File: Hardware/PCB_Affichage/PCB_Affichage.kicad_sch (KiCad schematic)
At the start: 0 parts

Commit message: finalisation PCB Rack
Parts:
- added C1, C5: 100n, Capacitor_SMD:C_0603_1608Metric_Pad1.08x0.95mm_HandSolder, symbol Device:C
- added C2: 1u, Capacitor_SMD:C_0201_0603Metric_Pad0.64x0.40mm_HandSolder, symbol Device:C
- added C3: 100u, Capacitor:Wurth-100u, symbol Device:C_Polarized
- added D1: TVS, Diode_SMD:Nexperia_DSN1608-2_1.6x0.8mm, symbol Diode:PTVS7V5Z1USK
- added D2: LED, LED_SMD:LED_0603_1608Metric_Pad1.05x0.95mm_HandSolder, symbol Device:LED
- added J1: Conn_01x03, Conn_Alim:Conn_Secteur, symbol Connector_Generic:Conn_01x03
- added R3: 2k5, Resistor_SMD:R_0603_1608Metric_Pad0.98x0.95mm_HandSolder, symbol Device:R
- added R5, R6: 2k2, Resistor_SMD:R_0603_1608Metric_Pad0.98x0.95mm_HandSolder, symbol Device:R
- added SW1: SW_SPST, Switch:Wurth_2pin_P5.0mm, symbol Switch:SW_SPST
- added U1: ~, ESP32_C3_SuperMini:C3_SuperMini, symbol ESP32_C3_SuperMini:SuperMini_1
- added U2: ~, AC_DC_module:MP-LDE06-20B05, symbol AC-DC-5V:U_1
- added U3: PCF8575DBR, Package_SO:SSOP-24_5.3x8.2mm_P0.65mm, symbol Interface_Expansion:PCF8575DBR
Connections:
- new net: D2.2 (A), R3.2
- new net +5V: C1.1, C2.1, C3.1, C5.2, D1.1 (K), R3.1, R5.1, R6.1, U1.8 (5V), U2.4 (DC+), U3.24 (VCC)
- new net Earth: J1.3 (Pin_3)
- new net GND: C1.2, C2.2, C3.2, C5.1, D1.2 (A), D2.1 (K), U1.7 (GND), U2.3 (DC-), U3.12 (GND), U3.2 (A1), U3.21 (A0), U3.3 (A2)
- new net INA1_1: U3.4 (P0)
- new net INA1_2: U3.5 (P1)
- new net INA2_1: U3.6 (P2)
- new net INA2_2: U3.7 (P3)
- new net INA3_1: U3.8 (P4)
- new net INA3_2: U3.9 (P5)
- new net INA4_1: U3.10 (P6)
- new net INA4_2: U3.11 (P7)
- new net INA5_1: U3.13 (P10)
- new net INA5_2: U3.14 (P11)
- new net INA6_1: U3.15 (P12)
- new net INA6_2: U3.16 (P13)
- new net LINE: SW1.1 (A), U2.2 (L)
- new net NEUT: J1.2 (Pin_2), U2.1 (N)
- new net On/Off: U1.14 (GPIO10)
- new net Phase: J1.1 (Pin_1), SW1.2 (B)
- new net Px: U1.9 (GPIO5)
- new net SCL: R5.2, U1.13 (GPIO9), U3.22 (SCL)
- new net SDA: R6.2, U1.12 (GPIO8), U3.23 (SDA)
- no-connect marks 0 -> 15
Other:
- note added: "Alimentation (230VAC)"
- note added: "Commande Neopixels"
- note added: "ESP32-C3"
- note added: "PSU AC/DC Input : 230V AC Output : 5V DC"

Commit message: finalisation PCB affichage
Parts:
- removed C2: 1u, Capacitor_SMD:C_0201_0603Metric_Pad0.64x0.40mm_HandSolder, symbol Device:C
- removed C3: 100u, Capacitor:Wurth-100u, symbol Device:C_Polarized
- removed C5: 100n, Capacitor_SMD:C_0603_1608Metric_Pad1.08x0.95mm_HandSolder, symbol Device:C
- removed D1: TVS, Diode_SMD:Nexperia_DSN1608-2_1.6x0.8mm, symbol Diode:PTVS7V5Z1USK
- removed J1: Conn_01x03, Conn_Alim:Conn_Secteur, symbol Connector_Generic:Conn_01x03
- removed R5, R6: 2k2, Resistor_SMD:R_0603_1608Metric_Pad0.98x0.95mm_HandSolder, symbol Device:R
- removed SW1: SW_SPST, Switch:Wurth_2pin_P5.0mm, symbol Switch:SW_SPST
- removed U1: ~, ESP32_C3_SuperMini:C3_SuperMini, symbol ESP32_C3_SuperMini:SuperMini_1
- removed U2: ~, AC_DC_module:MP-LDE06-20B05, symbol AC-DC-5V:U_1
- removed U3: PCF8575DBR, Package_SO:SSOP-24_5.3x8.2mm_P0.65mm, symbol Interface_Expansion:PCF8575DBR
- added J1: Conn_01x02, Connector_AMASS:AMASS_XT30U-F_1x02_P5.0mm_Vertical, symbol Connector_Generic:Conn_01x02
- added J2: Conn_01x03, Conn:MR30_F, symbol Connector_Generic:Conn_01x03
- added U2: ~, ESP32_SuperMini:SuperMini SMT, symbol ESP32_C3:SuperMini_1
- renumbered D2 to D1, R3 to R1
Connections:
- net +5V: now also J1.1 (Pin_1), J2.2 (Pin_2), U2.8 (5V)
- net GND: now also J1.2 (Pin_2), J2.3 (Pin_3), U2.7 (GND)
- net Px: now also J2.1 (Pin_1), U2.9 (GPIO5)
- no-connect marks 15 -> 13
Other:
- note added: "Connecteur Neopixels"
- note removed: "Commande Neopixels"
- note removed: "PSU AC/DC Input : 230V AC Output : 5V DC"
- moved on the sheet: C1, D1, R1

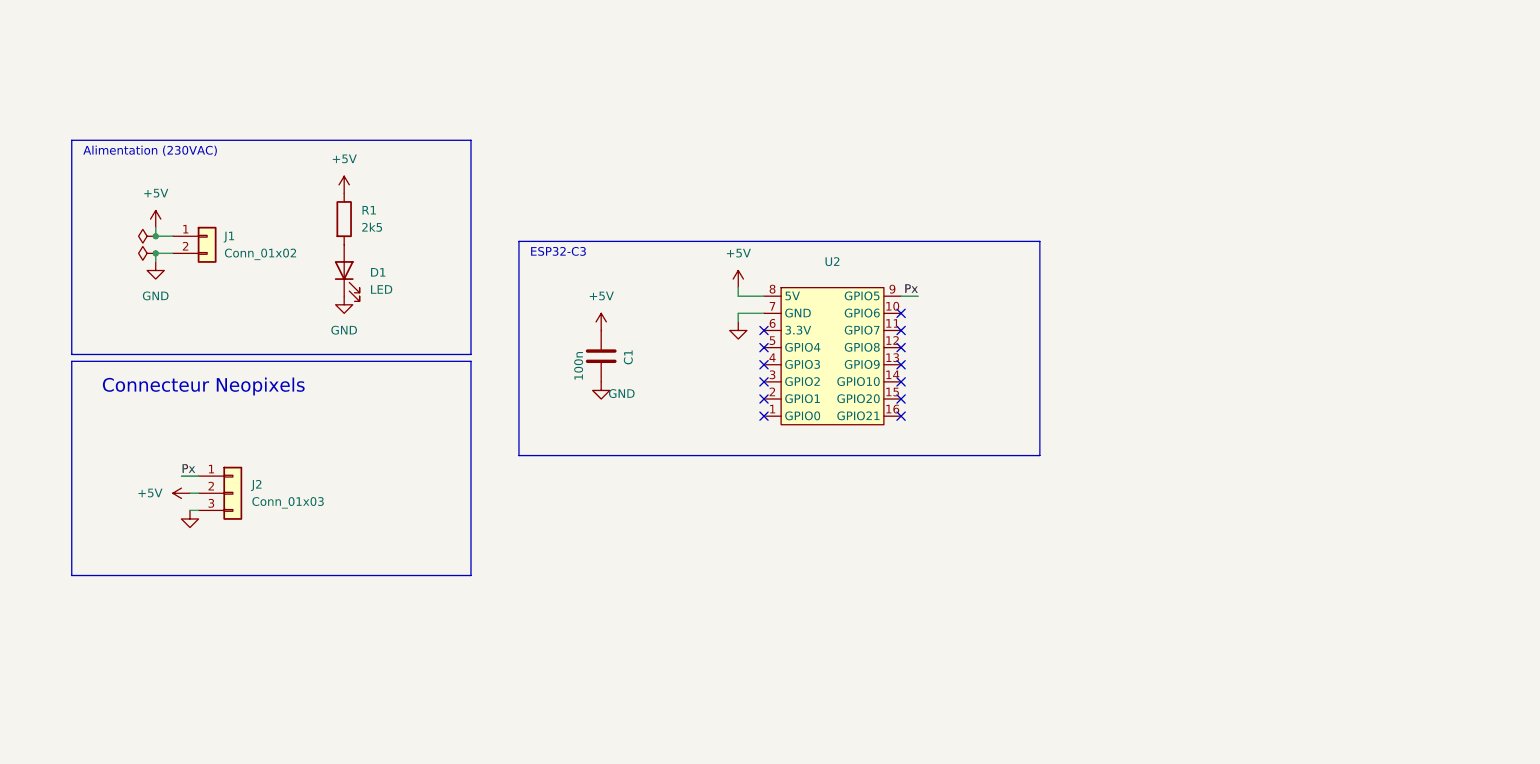
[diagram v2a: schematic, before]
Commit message: ajout des pinheaders en plus
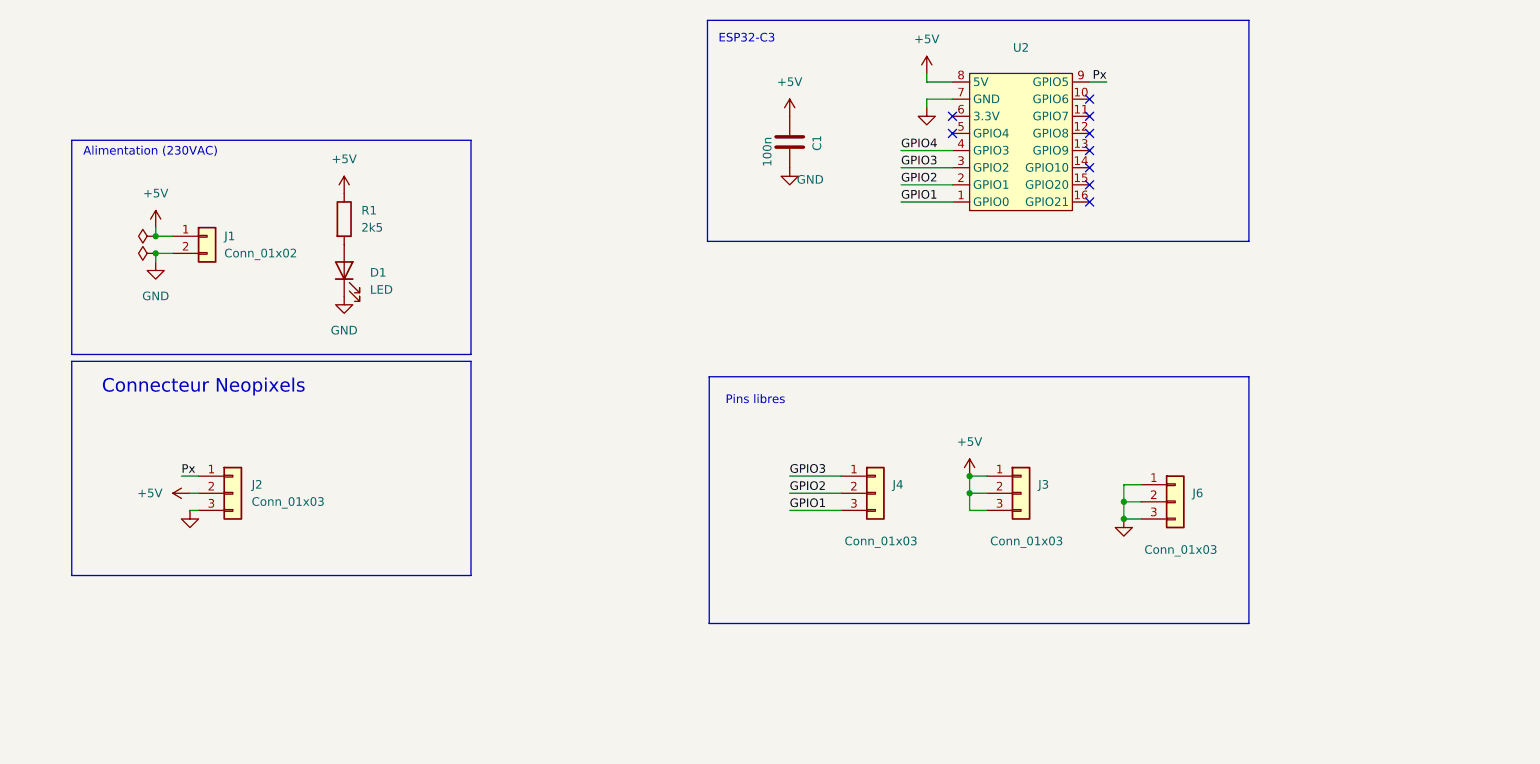
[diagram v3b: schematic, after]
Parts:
- added J3, J4, J6: Conn_01x03, Connector_PinHeader_2.54mm:PinHeader_1x03_P2.54mm_Vertical, symbol Connector_Generic:Conn_01x03
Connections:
- net +5V: now also J3.1 (Pin_1), J3.2 (Pin_2), J3.3 (Pin_3)
- net GND: now also J6.1 (Pin_1), J6.2 (Pin_2), J6.3 (Pin_3)
- net GPIO1: now reaches U2.1 (GPIO0)
- net GPIO1: now also J4.3 (Pin_3)
- net GPIO2: now reaches U2.2 (GPIO1)
- net GPIO2: now also J4.2 (Pin_2)
- net GPIO3: now reaches U2.3 (GPIO2)
- net GPIO3: now also J4.1 (Pin_1)
- net GPIO4: now reaches U2.4 (GPIO3)
- no-connect marks 13 -> 9
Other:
- note added: "Pins libres"
- moved on the sheet: C1, U2

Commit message: correction orientation des connecteurs sur secteur
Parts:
- D1: footprint LED_SMD:LED_0603_1608Metric_Pad1.05x0.95mm_HandSolder -> img:LED_0603_avec_dessin
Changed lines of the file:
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@@
 			)
 		)
-		(property "Footprint" "LED_SMD:LED_0603_1608Metric_Pad1.05x0.95mm_HandSolder"
+		(property "Footprint" "img:LED_0603_avec_dessin"
 			(at 62.23 50.8 0)
 			(effects
